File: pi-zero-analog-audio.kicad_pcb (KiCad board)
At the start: 2 copper layers, 65 x 30 mm, 38 parts, among them J1 GPIO, J2 Screw_Terminal_01x04, J3 Audio Jack, U1 MIC5365-3.3YD5, U2 MC74VHC1GT50, U3 MC74VHC1GT50, U4 PAM8403D

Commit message: vias to test AUD_3V3 for noise
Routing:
- net /AUD_3V3: track 18.7 -> 19.7 mm, vias 0 -> 3
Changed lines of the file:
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@@
     (property "ki_keywords" "cap capacitor")
     (attr smd)
-    (fp_text reference "C15" (at 0 -0.073 -180) (layer "F.SilkS")
+    (fp_text reference "C15" (at 0.073 -0.073 -180) (layer "F.SilkS")
         (effects (font (size 0.5 0.5) (thickness 0.125)))
     )
@@
   (segment (start 119.6105 91.17) (end 119.6105 93.1645) (width 0.508) (layer "F.Cu") (net 30))
   (segment (start 121.752 91.17) (end 119.6105 91.17) (width 0.508) (layer "F.Cu") (net 30))
-  (segment (start 109.982 83.566) (end 109.982 81.026) (width 0.508) (layer "F.Cu") (net 31))
-  (segment (start 109.982 81.026) (end 110.4685 80.5395) (width 0.508) (layer "F.Cu") (net 31))
+  (segment (start 111.586 80.5395) (end 110.4685 80.5395) (width 0.508) (layer "F.Cu") (net 31))
+  (segment (start 110.4685 80.5395) (end 109.982 81.026) (width 0.508) (layer "F.Cu") (net 31))
+  (segment (start 111.7525 89.1595) (end 109.982 87.389) (width 0.508) (layer "F.Cu") (net 31))
+  (segment (start 108.3775 81.374) (end 108.3775 81.809) (width 0.508) (layer "F.Cu") (net 31))
+  (segment (start 109.982 87.389) (end 109.982 83.566) (width 0.508) (layer "F.Cu") (net 31))
+  (segment (start 109.982 81.026) (end 109.982 83.566) (width 0.508) (layer "F.Cu") (net 31))
   (segment (start 111.84 89.072) (end 114.2125 89.072) (width 0.508) (layer "F.Cu") (net 31))
-  (segment (start 109.982 87.389) (end 109.982 83.566) (width 0.508) (layer "F.Cu") (net 31))
-  (segment (start 110.4685 80.5395) (end 111.586 80.5395) (width 0.508) (layer "F.Cu") (net 31))
+  (segment (start 108.305 81.3015) (end 108.3775 81.374) (width 0.508) (layer "F.Cu") (net 31))
   (segment (start 109.982 83.566) (end 109.909 83.639) (width 0.508) (layer "F.Cu") (net 31))
-  (segment (start 108.3775 83.639) (end 108.3775 81.809) (width 0.508) (layer "F.Cu") (net 31))
+  (segment (start 108.3775 83.639) (end 108.3775 81.374) (width 0.508) (layer "F.Cu") (net 31))
   (segment (start 111.731 80.6845) (end 113.966 80.6845) (width 0.508) (layer "F.Cu") (net 31))
   (segment (start 109.909 83.639) (end 108.3775 83.639) (width 0.508) (layer "F.Cu") (net 31))
-  (segment (start 111.7525 89.1595) (end 109.982 87.389) (width 0.508) (layer "F.Cu") (net 31))
+  (via (at 111.7525 89.1595) (size 0.9) (drill 0.6) (layers "F.Cu" "B.Cu") (net 31))
+  (via (at 111.586 80.5395) (size 0.9) (drill 0.6) (layers "F.Cu" "B.Cu") (net 31))
+  (via (at 108.305 81.3015) (size 0.9) (drill 0.6) (layers "F.Cu" "B.Cu") (net 31))
   (segment (start 136.287104 81.962396) (end 131.6655 86.584) (width 0.508) (layer "F.Cu") (net 32))
   (segment (start 143.721 81.962396) (end 136.287104 81.962396) (width 0.508) (layer "F.Cu") (net 32))

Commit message: DRC run
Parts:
- removed MUTE, SHDN: SolderJumper_2_Bridged, Jumper:SolderJumper-2_P1.3mm_Bridged_RoundedPad1.0x1.5mm
- added JP1: SolderJumper_2_Bridged, Jumper:SolderJumper-2_P1.3mm_Bridged_RoundedPad1.0x1.5mm, B.Cu at (157.0, 79.8)
- added JP2: SolderJumper_2_Bridged, Jumper:SolderJumper-2_P1.3mm_Bridged_RoundedPad1.0x1.5mm, B.Cu at (154.4, 79.8)
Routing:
- net /AUD_3V3: track 19.7 -> 19.2 mm
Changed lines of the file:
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@@
     (attr exclude_from_pos_files)
     (net_tie_pad_groups "1, 2")
-    (fp_text reference "SHDN" (at 1.016 -3.048 180) (layer "B.SilkS")
-        (effects (font (size 1 1) (thickness 0.15)) (justify mirror))
+    (fp_text reference "JP1" (at -2.032 0 180) (layer "B.SilkS")
+        (effects (font (size 0.5 0.5) (thickness 0.1) bold) (justify mirror))
     )
     (fp_text value "SolderJumper_2_Bridged" (at 0 -1.9 90) (layer "B.Fab")
@@
     (attr exclude_from_pos_files)
     (net_tie_pad_groups "1, 2")
-    (fp_text reference "MUTE" (at 1.016 3.048 180) (layer "B.SilkS")
-        (effects (font (size 1 1) (thickness 0.15)) (justify mirror))
+    (fp_text reference "JP2" (at -2.032 0 180) (layer "B.SilkS")
+        (effects (font (size 0.5 0.5) (thickness 0.1) bold) (justify mirror))
     )
     (fp_text value "SolderJumper_2_Bridged" (at 0 -1.9 90) (layer "B.Fab")
@@
   (segment (start 110.4685 80.5395) (end 109.982 81.026) (width 0.508) (layer "F.Cu") (net 31))
   (segment (start 111.7525 89.1595) (end 109.982 87.389) (width 0.508) (layer "F.Cu") (net 31))
-  (segment (start 108.3775 81.374) (end 108.3775 81.809) (width 0.508) (layer "F.Cu") (net 31))
   (segment (start 109.982 87.389) (end 109.982 83.566) (width 0.508) (layer "F.Cu") (net 31))
   (segment (start 109.982 81.026) (end 109.982 83.566) (width 0.508) (layer "F.Cu") (net 31))
   (segment (start 111.84 89.072) (end 114.2125 89.072) (width 0.508) (layer "F.Cu") (net 31))
-  (segment (start 108.305 81.3015) (end 108.3775 81.374) (width 0.508) (layer "F.Cu") (net 31))
   (segment (start 109.982 83.566) (end 109.909 83.639) (width 0.508) (layer "F.Cu") (net 31))
   (segment (start 108.3775 83.639) (end 108.3775 81.374) (width 0.508) (layer "F.Cu") (net 31))
   (segment (start 111.731 80.6845) (end 113.966 80.6845) (width 0.508) (layer "F.Cu") (net 31))
   (segment (start 109.909 83.639) (end 108.3775 83.639) (width 0.508) (layer "F.Cu") (net 31))
-  (via (at 111.7525 89.1595) (size 0.9) (drill 0.6) (layers "F.Cu" "B.Cu") (net 31))
-  (via (at 111.586 80.5395) (size 0.9) (drill 0.6) (layers "F.Cu" "B.Cu") (net 31))
-  (via (at 108.305 81.3015) (size 0.9) (drill 0.6) (layers "F.Cu" "B.Cu") (net 31))
+  (via locked (at 111.7525 89.1595) (size 0.9) (drill 0.6) (layers "F.Cu" "B.Cu") (net 31))
+  (via locked (at 111.586 80.5395) (size 0.9) (drill 0.6) (layers "F.Cu" "B.Cu") (net 31))
+  (via locked (at 108.305 81.3015) (size 0.9) (drill 0.6) (layers "F.Cu" "B.Cu") (net 31))
   (segment (start 136.287104 81.962396) (end 131.6655 86.584) (width 0.508) (layer "F.Cu") (net 32))
   (segment (start 143.721 81.962396) (end 136.287104 81.962396) (width 0.508) (layer "F.Cu") (net 32))

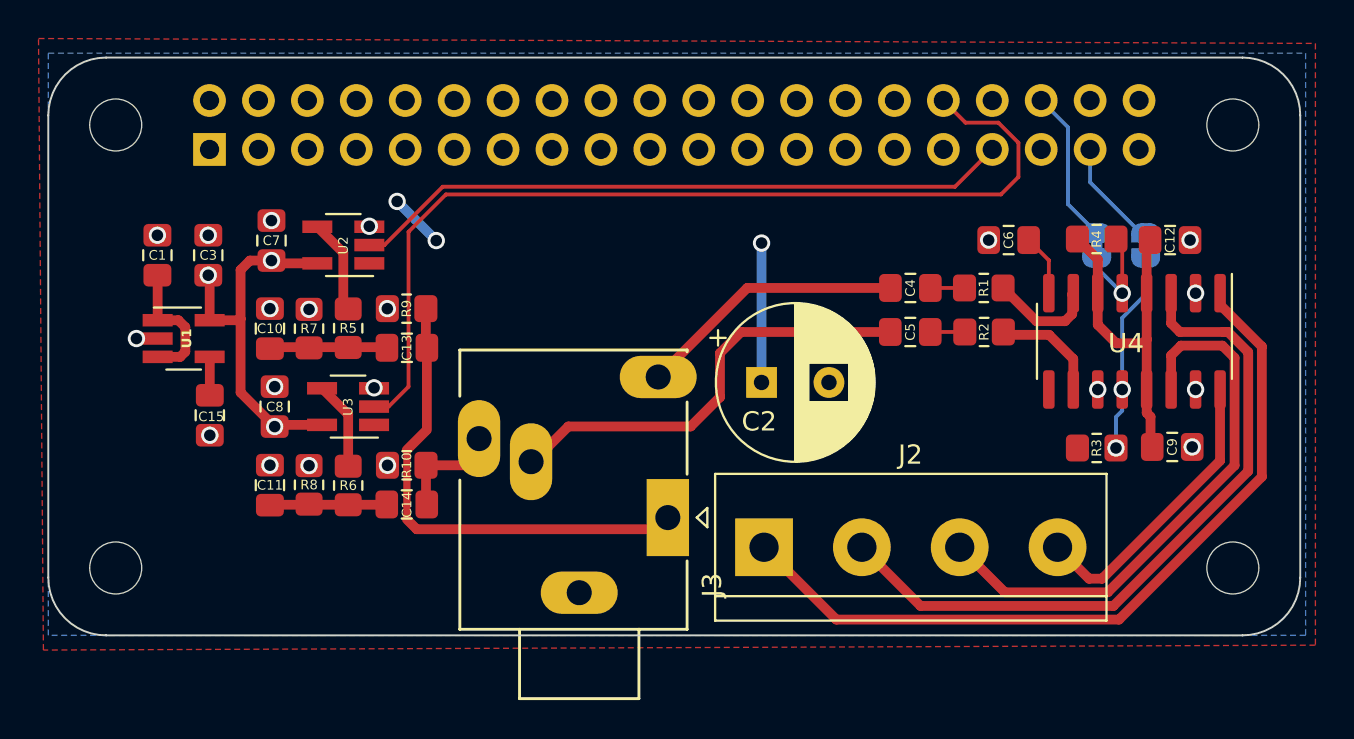
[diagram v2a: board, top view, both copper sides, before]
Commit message: Adding ferrite beads on 3V3 rails
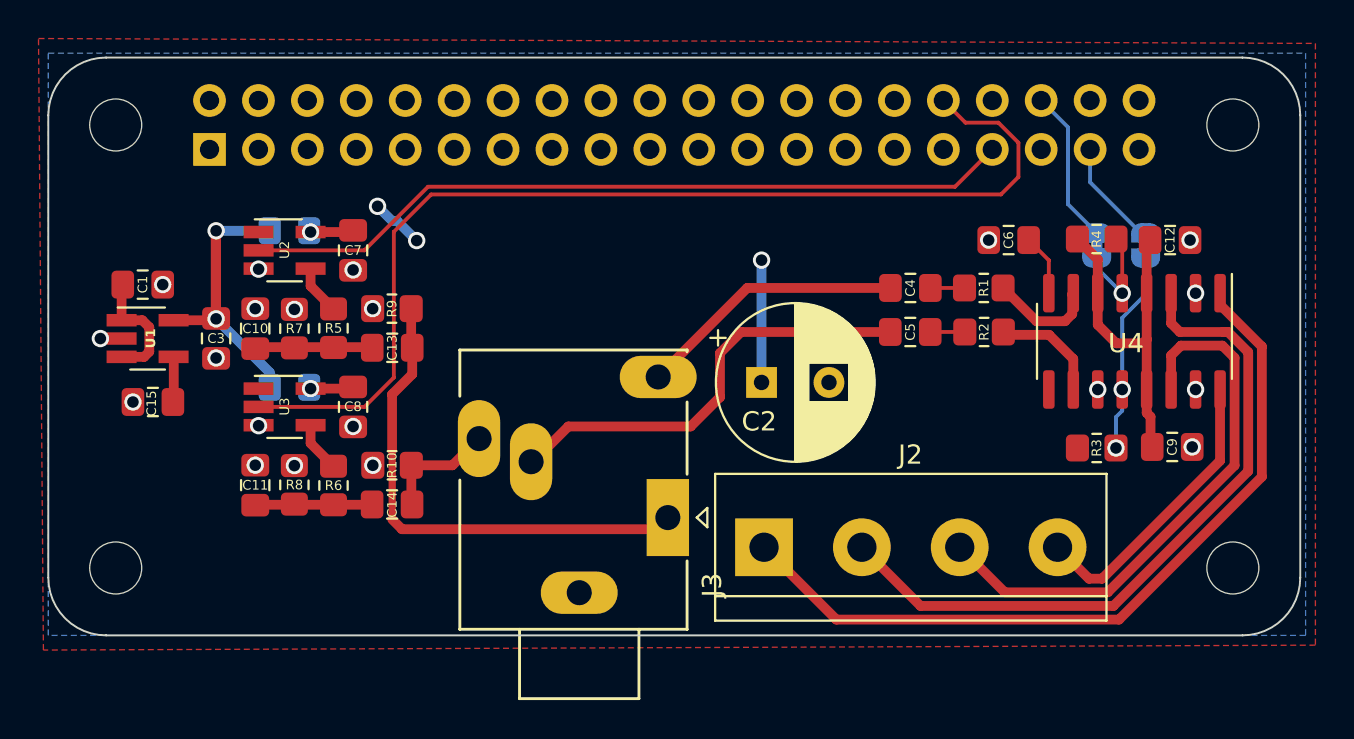
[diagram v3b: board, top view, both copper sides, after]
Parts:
- added FB1: FerriteBead, PCM_Ferrite_SMD_Handsoldering_AKL:Ferrite_0805_2012Metric_Pad1.15x1.40mm_BigPads, B.Cu at (112.5, 79.0)
- added FB2: FerriteBead, PCM_Ferrite_SMD_Handsoldering_AKL:Ferrite_0805_2012Metric_Pad1.15x1.40mm_BigPads, B.Cu at (112.5, 87.1)
- moved C3 4.34 mm to (108.7, 84.6), turned to -90 degrees
- moved C7 4.27 mm to (115.8, 80.0), turned to -90 degrees
- moved C8 4.07 mm to (115.8, 88.1), turned to -90 degrees
- moved U3 3.29 mm to (112.3, 88.1), turned to 0 degrees
- moved U2 3.06 mm to (112.3, 80.0), turned to 0 degrees
- moved C15 3.03 mm to (105.4, 87.9), turned to 180 degrees
- moved U1 1.87 mm to (105.2, 84.6)
- moved C1 1.70 mm to (104.9, 81.8), turned to 0 degrees
- moved C10 0.76 mm to (110.7, 84.1)
- moved C11 0.76 mm to (110.7, 92.2)
- moved C13 0.76 mm to (117.9, 85.1)
- moved C14 0.76 mm to (117.8, 93.2)
- moved R10 0.76 mm to (117.8, 91.2)
- moved R7 0.76 mm to (112.8, 84.1)
- moved R8 0.76 mm to (112.8, 92.2)
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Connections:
- C7 pad 1: /AUD_3V3 -> Net-(U2-VCC)
- C8 pad 1: /AUD_3V3 -> Net-(U3-VCC)
- U2 pad 5: /AUD_3V3 -> Net-(U2-VCC)
- U3 pad 5: /AUD_3V3 -> Net-(U3-VCC)
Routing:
- net /PWM0: track 49.7 -> 55.4 mm
- net /PWM1: track 34.4 -> 40.0 mm
- net Net-(U3-VCC): track 0.00 -> 2.12 mm, vias 0 -> 1
- net Net-(U2-VCC): track 0.00 -> 2.12 mm, vias 0 -> 1
- net Net-(U2-Y): track 4.57 -> 2.59 mm
- net Net-(U3-Y): track 4.61 -> 2.62 mm
- net /AUDIO_R: track 4.14 -> 6.09 mm
- net +5V: track 34.8 -> 33.8 mm
- net /AUDIO_L: track 24.5 -> 25.2 mm
- net /AUD_3V3: track 19.2 -> 18.7 mm, vias 3 -> 2

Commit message: shorter traces
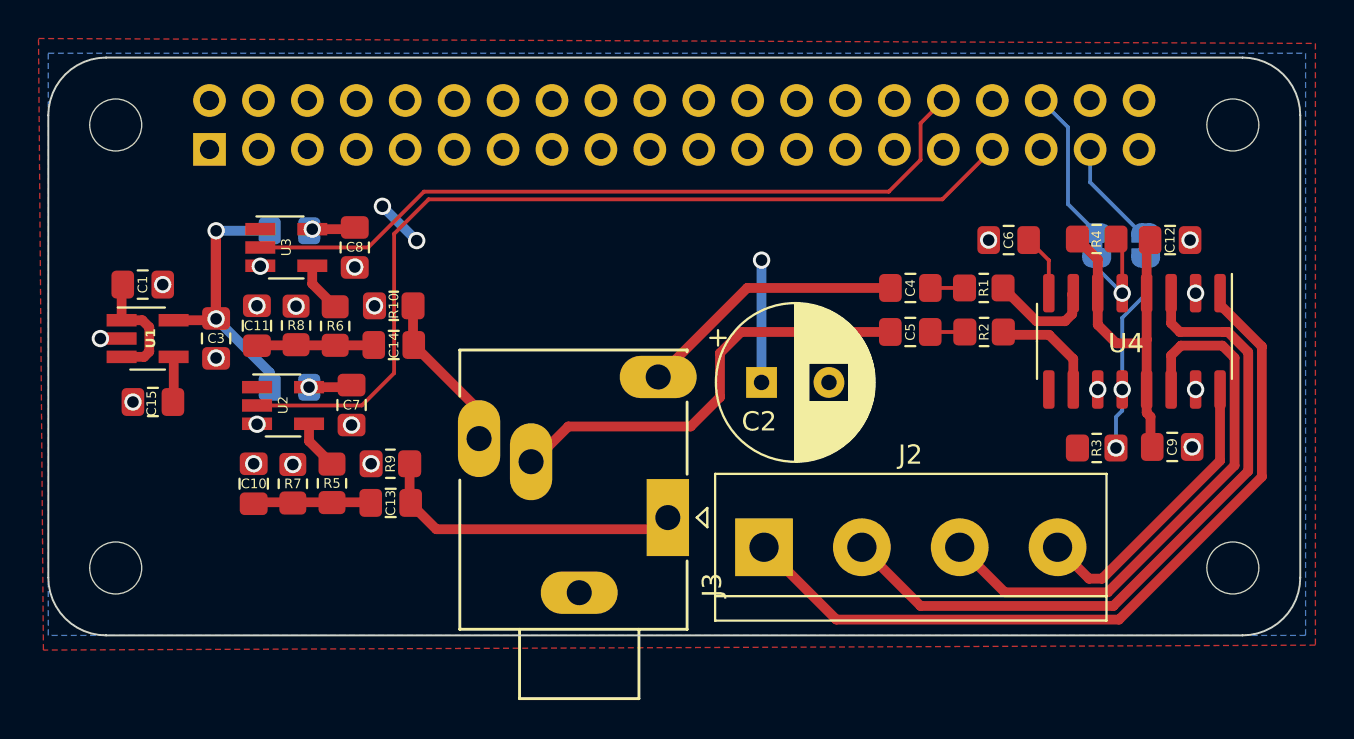
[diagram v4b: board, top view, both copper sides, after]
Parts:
- moved C8 8.28 mm to (115.9, 79.9)
- moved R10 8.28 mm to (117.9, 82.9)
- moved R8 8.28 mm to (112.9, 83.9)
- moved U3 8.28 mm to (112.4, 79.9)
- moved R6 8.28 mm to (114.9, 83.9)
- moved C11 8.28 mm to (110.8, 83.9)
- moved C14 8.28 mm to (117.9, 84.9)
- moved FB1 8.13 mm to (112.5, 87.1)
- moved FB2 8.13 mm to (112.5, 79.0)
- moved C10 8.05 mm to (110.7, 92.1)
- moved C13 8.05 mm to (117.8, 93.1)
- moved R5 8.05 mm to (114.7, 92.1)
- moved R7 8.05 mm to (112.7, 92.1)
- moved R9 8.05 mm to (117.8, 91.1)
- moved U2 8.05 mm to (112.2, 88.1)
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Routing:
- net /PWM0: track 55.4 -> 39.7 mm
- net /AUDIO_L: track 25.2 -> 15.3 mm
- net /PWM1: track 40.0 -> 47.7 mm
- net /AUDIO_R: track 6.09 -> 6.79 mm

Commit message: nit-picking
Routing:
- net /AUDIO_R: track 6.79 -> 8.26 mm
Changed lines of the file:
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@@
   (segment (start 117.348 77.724) (end 119.126 79.502) (width 0.508) (layer "B.Cu") (net 26))
   (segment (start 137.031349 80.518) (end 137.031349 86.868) (width 0.508) (layer "B.Cu") (net 26))
-  (segment (start 120.142 94.488) (end 131.5615 94.488) (width 0.508) (layer "F.Cu") (net 29))
+  (segment (start 118.8135 93.1595) (end 119.538 93.884) (width 0.508) (layer "F.Cu") (net 29))
+  (segment (start 119.538 93.884) (end 132.1655 93.884) (width 0.508) (layer "F.Cu") (net 29))
   (segment (start 118.76 91.09) (end 118.76 93.0685) (width 0.508) (layer "F.Cu") (net 29))
-  (segment (start 120.142 94.488) (end 118.8135 93.1595) (width 0.508) (layer "F.Cu") (net 29))
+  (segment (start 118.973 86.3915) (end 122.3655 89.784) (width 0.508) (layer "F.Cu") (net 30))
   (segment (start 118.9355 82.892) (end 118.9355 84.8865) (width 0.508) (layer "F.Cu") (net 30))
-  (segment (start 118.973 84.924) (end 122.3655 88.3165) (width 0.508) (layer "F.Cu") (net 30))
+  (segment (start 118.973 84.924) (end 118.973 86.3915) (width 0.508) (layer "F.Cu") (net 30))
   (segment (start 108.6905 79.0155) (end 108.712 78.994) (width 0.2) (layer "F.Cu") (net 31))
   (segment (start 106.506 83.639) (end 108.6175 83.639) (width 0.508) (layer "F.Cu") (net 31))

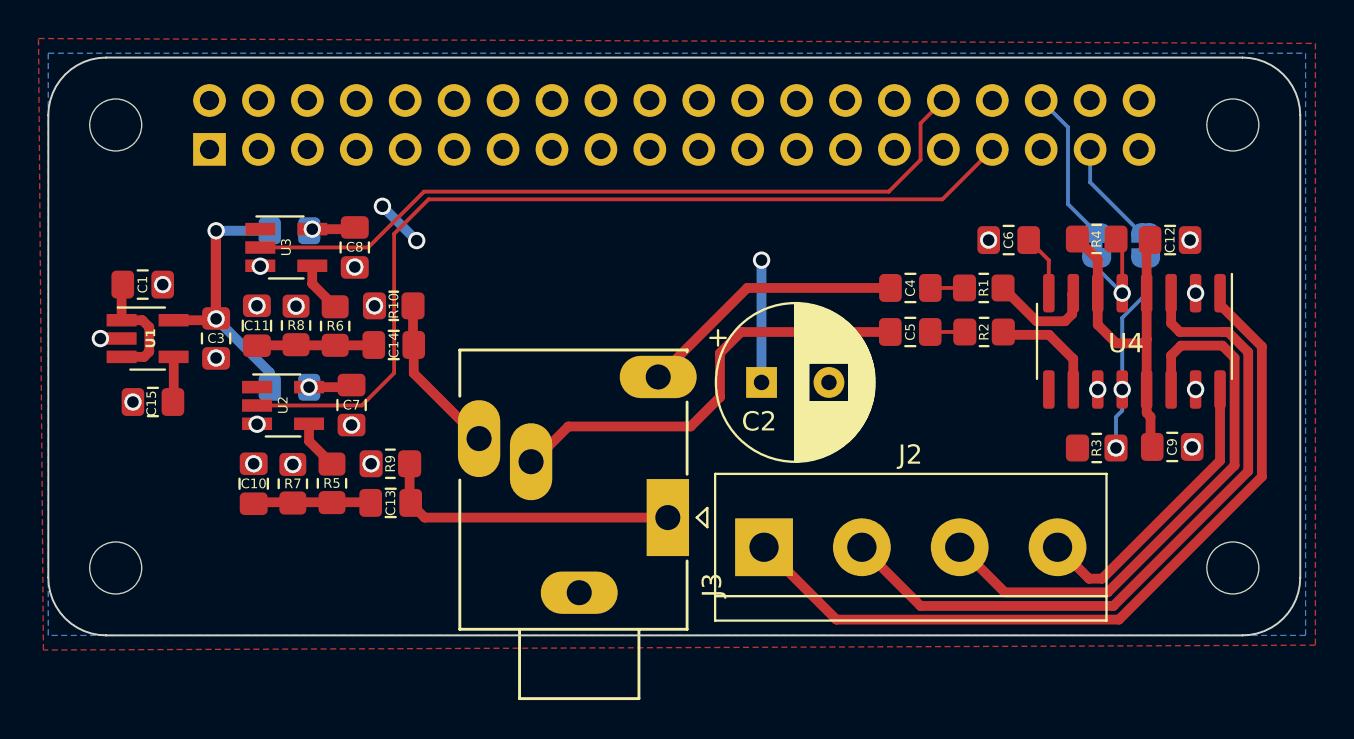
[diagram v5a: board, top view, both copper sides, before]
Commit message: More ground zones trying to isolate 3V3 traces
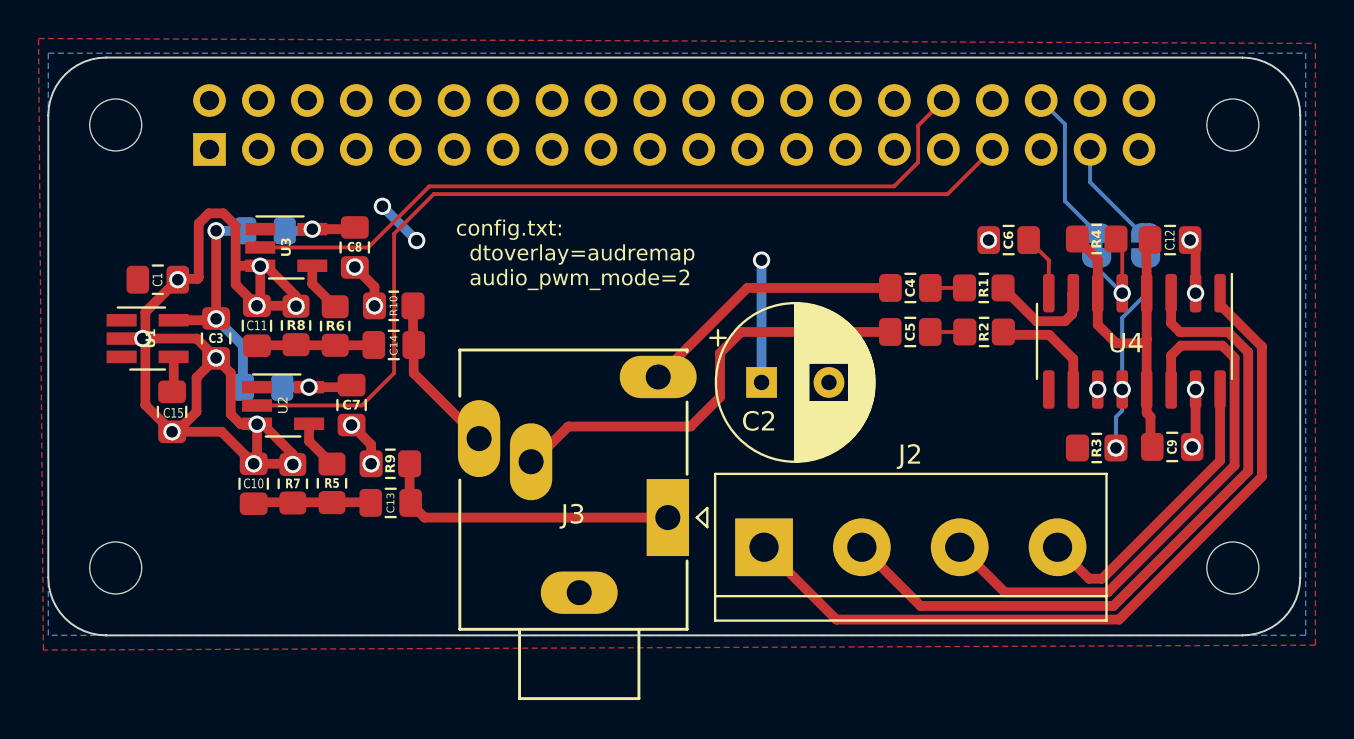
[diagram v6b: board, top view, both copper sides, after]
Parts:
- moved FB1 1.40 mm to (111.1, 87.1)
- moved FB2 1.27 mm to (111.3, 79.0)
- moved C15 1.12 mm to (106.4, 88.4), turned to -90 degrees
- moved C1 0.82 mm to (105.7, 81.5)
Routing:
- net GND: track 0.00 -> 63.0 mm
- net /AUD_3V3: track 18.7 -> 12.2 mm
- net +5V: track 33.6 -> 27.3 mm
- net Net-(U3-VCC): track 2.12 -> 3.50 mm
- net Net-(U2-VCC): track 2.12 -> 3.26 mm
- added copper zone on F.Cu, net GND
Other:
- board text added: "config.txt: dtoverlay=audremap audio_pwm_mode=2"

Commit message: Two GND zones
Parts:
- moved FB1 1.82 mm to (111.5, 85.3)
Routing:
- net +5V: track 27.3 -> 103.7 mm, vias 3 -> 0
- net GND: track 63.0 -> 72.6 mm
- net Net-(JP1-B): track 10.5 -> 13.2 mm
- net Net-(C10-Pad1): track 6.04 -> 8.04 mm
- net /AUD_3V3: track 12.2 -> 10.7 mm
- net /SHDN: track 5.42 -> 6.69 mm
- net Net-(U4-INL): track 5.60 -> 6.63 mm
- net Net-(U2-VCC): track 3.26 -> 4.28 mm
- net Net-(U1-NC): track 1.99 -> 2.72 mm
- net /AUDIO_L: track 15.6 -> 16.2 mm
- removed copper zone on F.Cu, net +5V

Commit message: Revert "Two GND zones"
This reverts commit edaad1ef0305b16592a24cacb57811a0cb0df8b8.
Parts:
- moved FB1 1.82 mm to (111.1, 87.1)
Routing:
- net +5V: track 103.7 -> 27.3 mm, vias 0 -> 3
- net GND: track 72.6 -> 63.0 mm
- net Net-(JP1-B): track 13.2 -> 10.5 mm
- net Net-(C10-Pad1): track 8.04 -> 6.04 mm
- net /AUD_3V3: track 10.7 -> 12.2 mm
- net /SHDN: track 6.69 -> 5.42 mm
- net Net-(U4-INL): track 6.63 -> 5.60 mm
- net Net-(U2-VCC): track 4.28 -> 3.26 mm
- net Net-(U1-NC): track 2.72 -> 1.99 mm
- net /AUDIO_L: track 16.2 -> 15.6 mm
- added copper zone on F.Cu, net +5V
